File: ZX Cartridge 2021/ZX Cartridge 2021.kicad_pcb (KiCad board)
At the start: 2 copper layers, 57.9 x 61.6 mm, 13 parts, among them J1 Cartridge, M1 Mounting, M2 Mounting, M3 Mounting, M4 Mounting, U1 27C512, U2 27C512

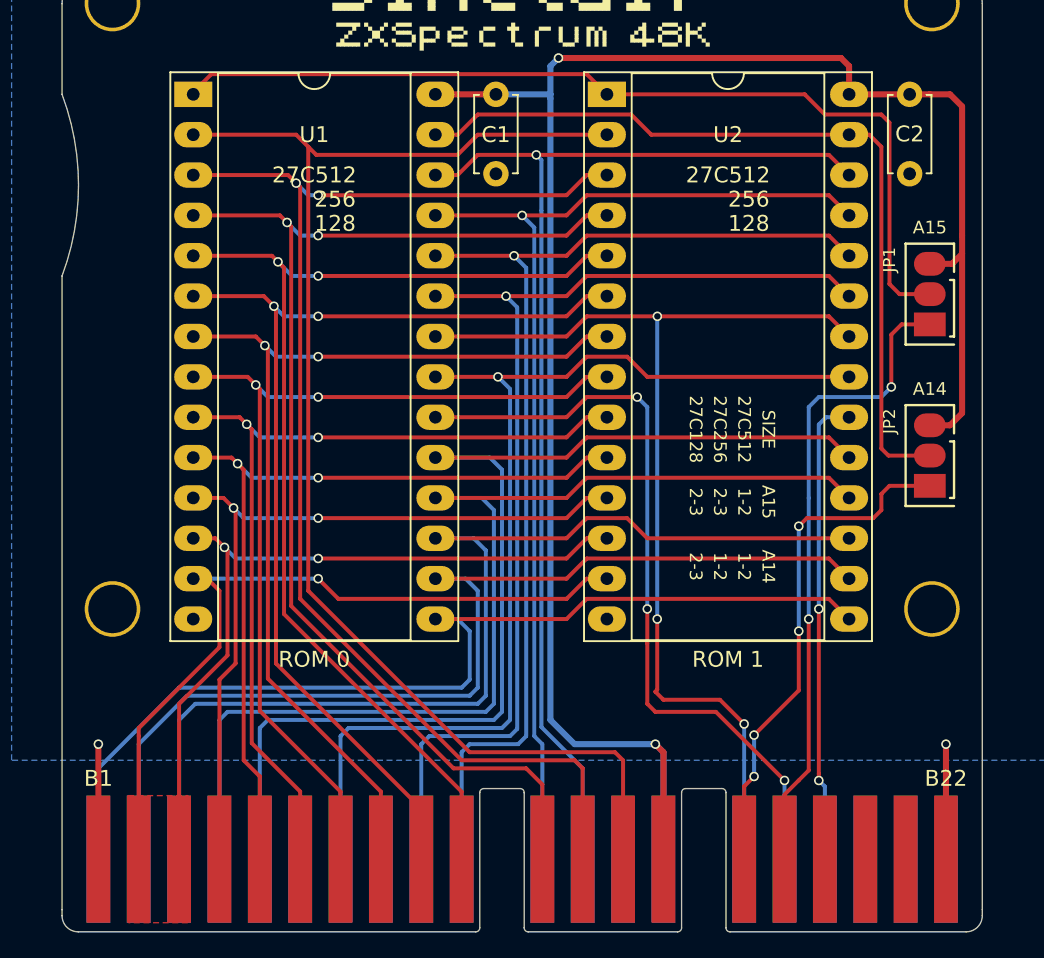
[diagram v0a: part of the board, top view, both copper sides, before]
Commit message: Fixed cartridge pinout
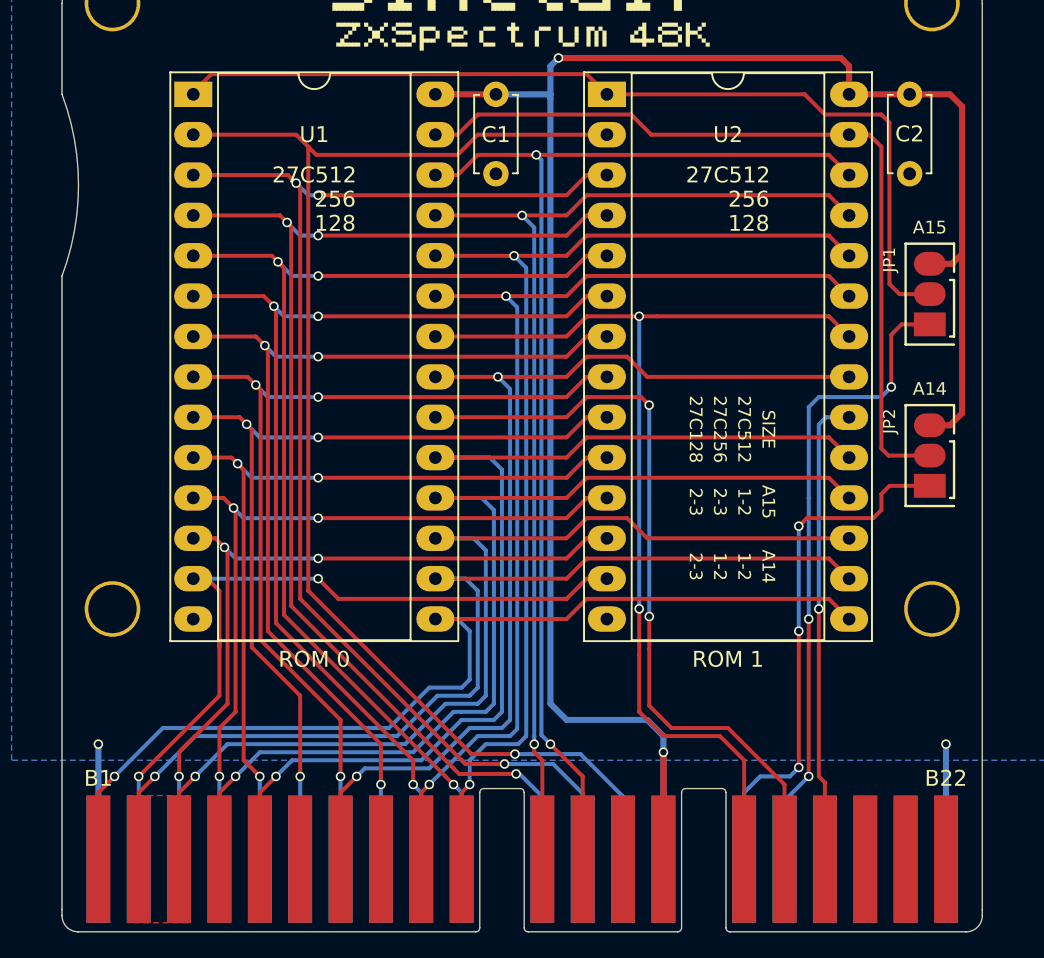
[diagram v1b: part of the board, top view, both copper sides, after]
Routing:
- net /D6: track 69.7 -> 67.1 mm, vias 0 -> 1
- net /D5: track 68.4 -> 65.7 mm, vias 0 -> 1
- net /D7: track 70.7 -> 68.4 mm, vias 0 -> 1
- net /A10: track 67.8 -> 65.7 mm, vias 1 -> 2
- net /A11: track 68.3 -> 66.5 mm, vias 1 -> 2
- net /D4: track 66.2 -> 64.4 mm, vias 0 -> 1
- net VCC: track 122.9 -> 121.2 mm
- net /A12: track 85.5 -> 84.1 mm, vias 0 -> 1
- net Net-(J1-PadB17): track 32.3 -> 33.4 mm, vias 4 -> 3
- net /A9: track 69.2 -> 68.2 mm, vias 1 -> 2
- net /A7: track 81.3 -> 80.3 mm, vias 2 -> 3
- net /D3: track 64.0 -> 63.1 mm, vias 0 -> 1
- net /D2: track 48.0 -> 48.6 mm, vias 1 -> 2
- net /A6: track 76.5 -> 76.0 mm, vias 2 -> 3
- net /~ROM_OE: track 65.7 -> 66.1 mm, vias 3 -> 2
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
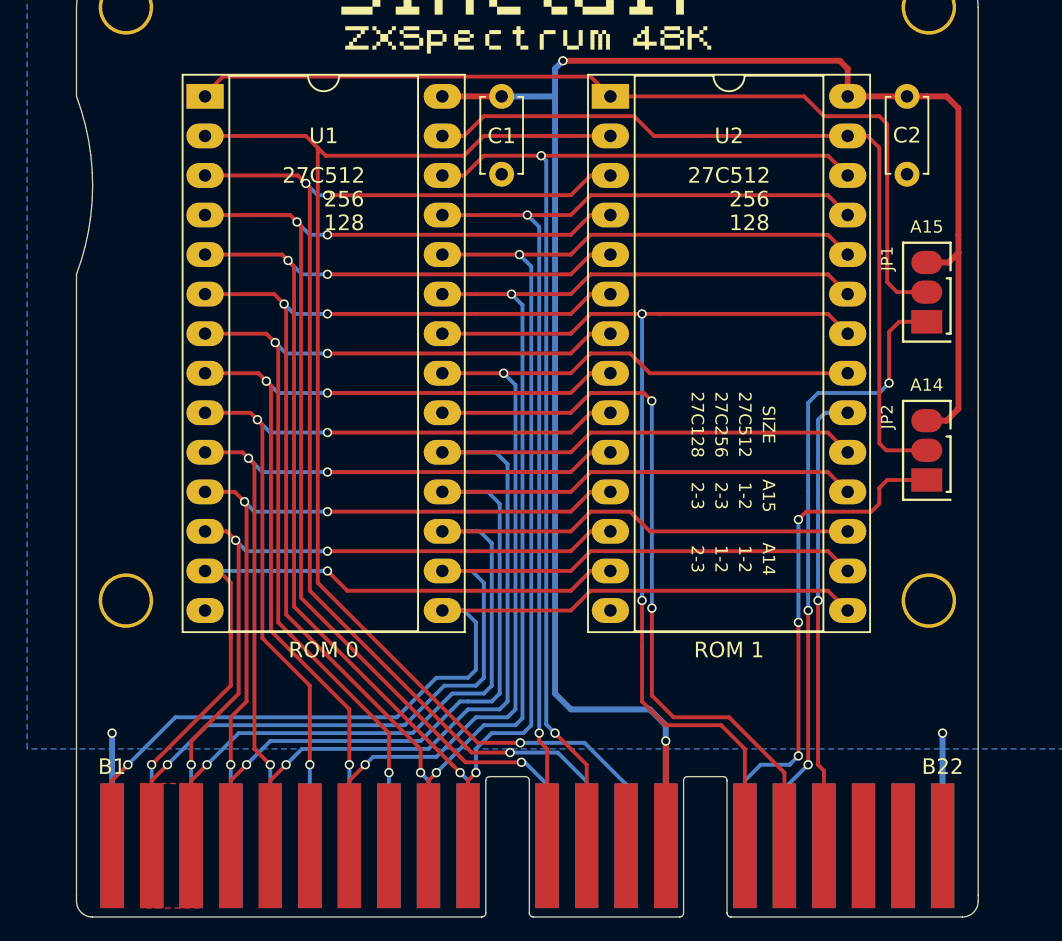
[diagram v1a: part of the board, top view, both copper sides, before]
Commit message: Fixed diagnostic pinout
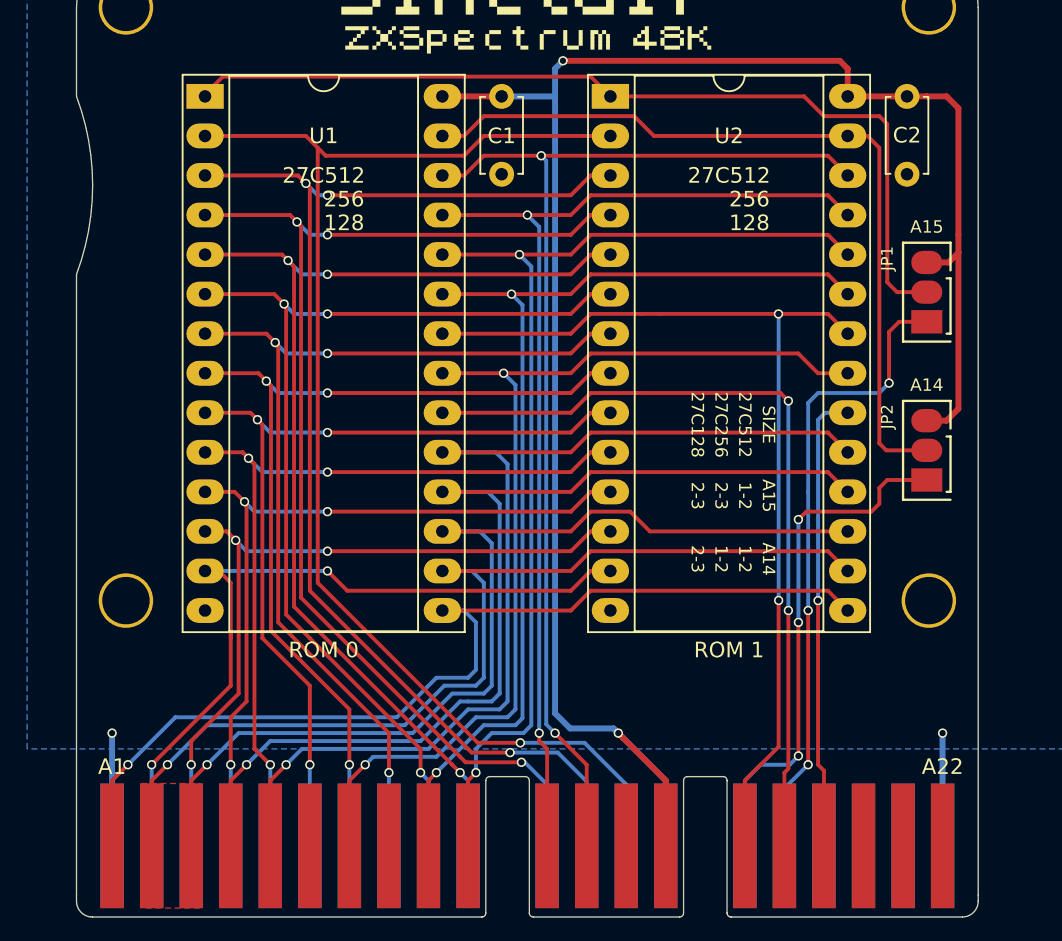
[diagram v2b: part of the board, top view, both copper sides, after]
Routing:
- net /~ROM_OE: track 66.1 -> 62.2 mm
- net /~ROM_0: track 48.4 -> 51.6 mm
